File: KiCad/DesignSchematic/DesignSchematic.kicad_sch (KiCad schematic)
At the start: 17 parts, among them M1 Motor_DC, M2 Motor_DC, U1 EDU-CIAA, U2 AS5600, U3 AS5600, U4 MT3608, U5 VL53L0X, U6 DVR-8833, U7 MPU6050, U8 NodeMCU3.0(ESP-12E)

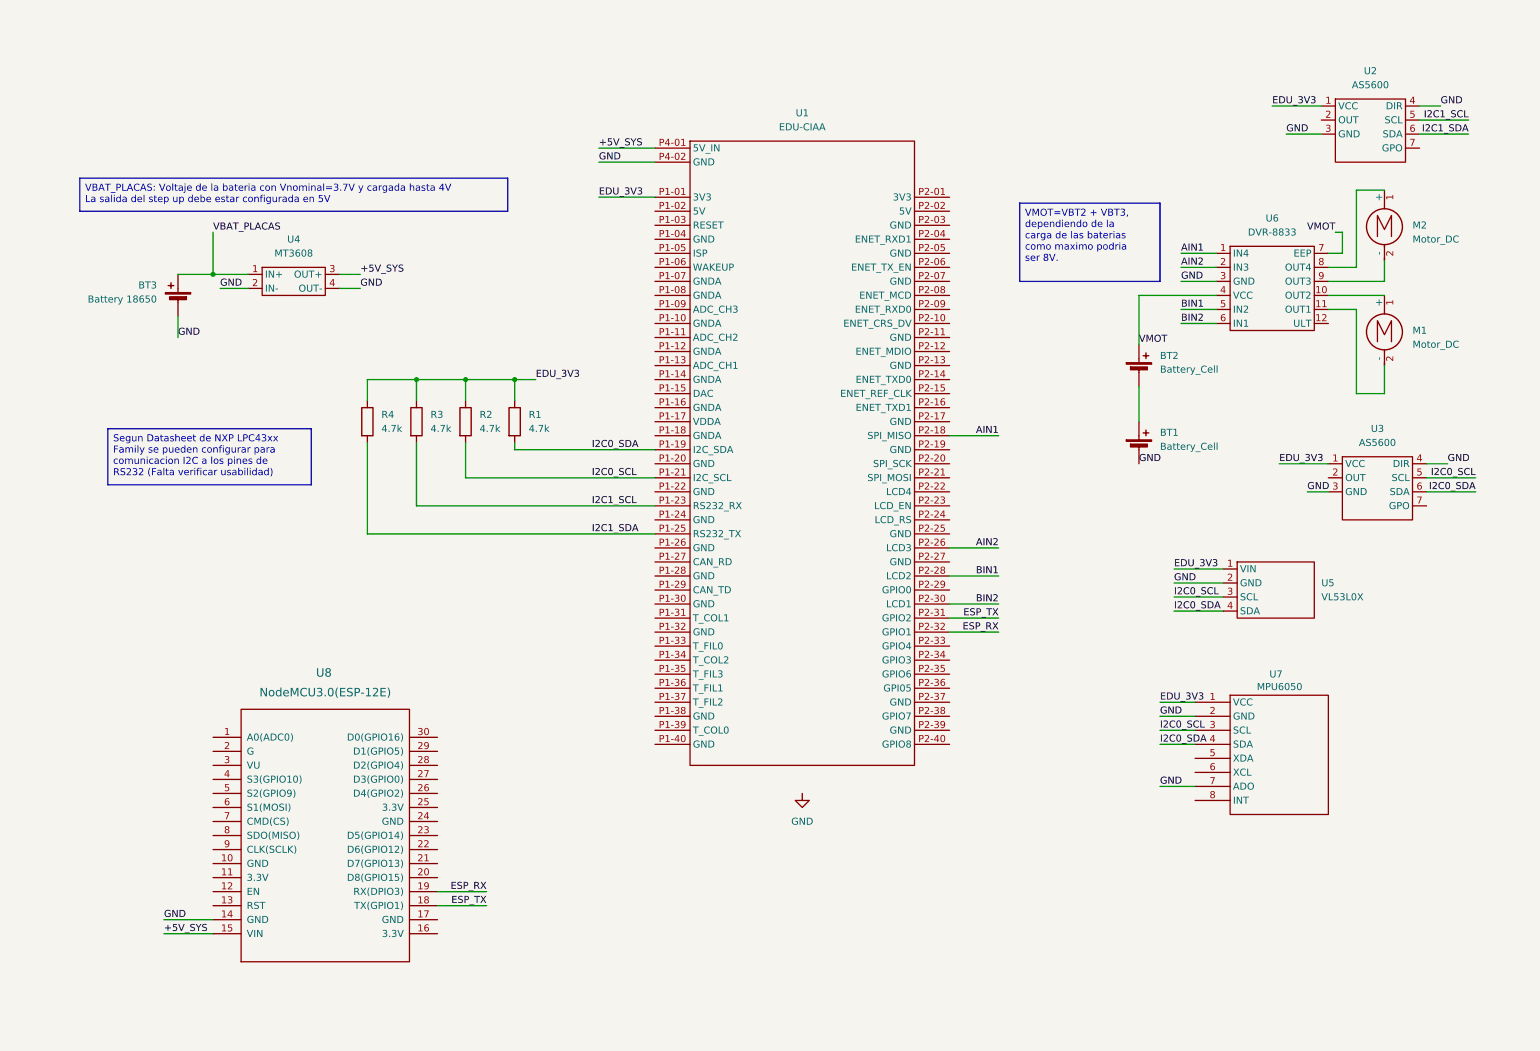
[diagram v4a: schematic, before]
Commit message: modificando esquematico
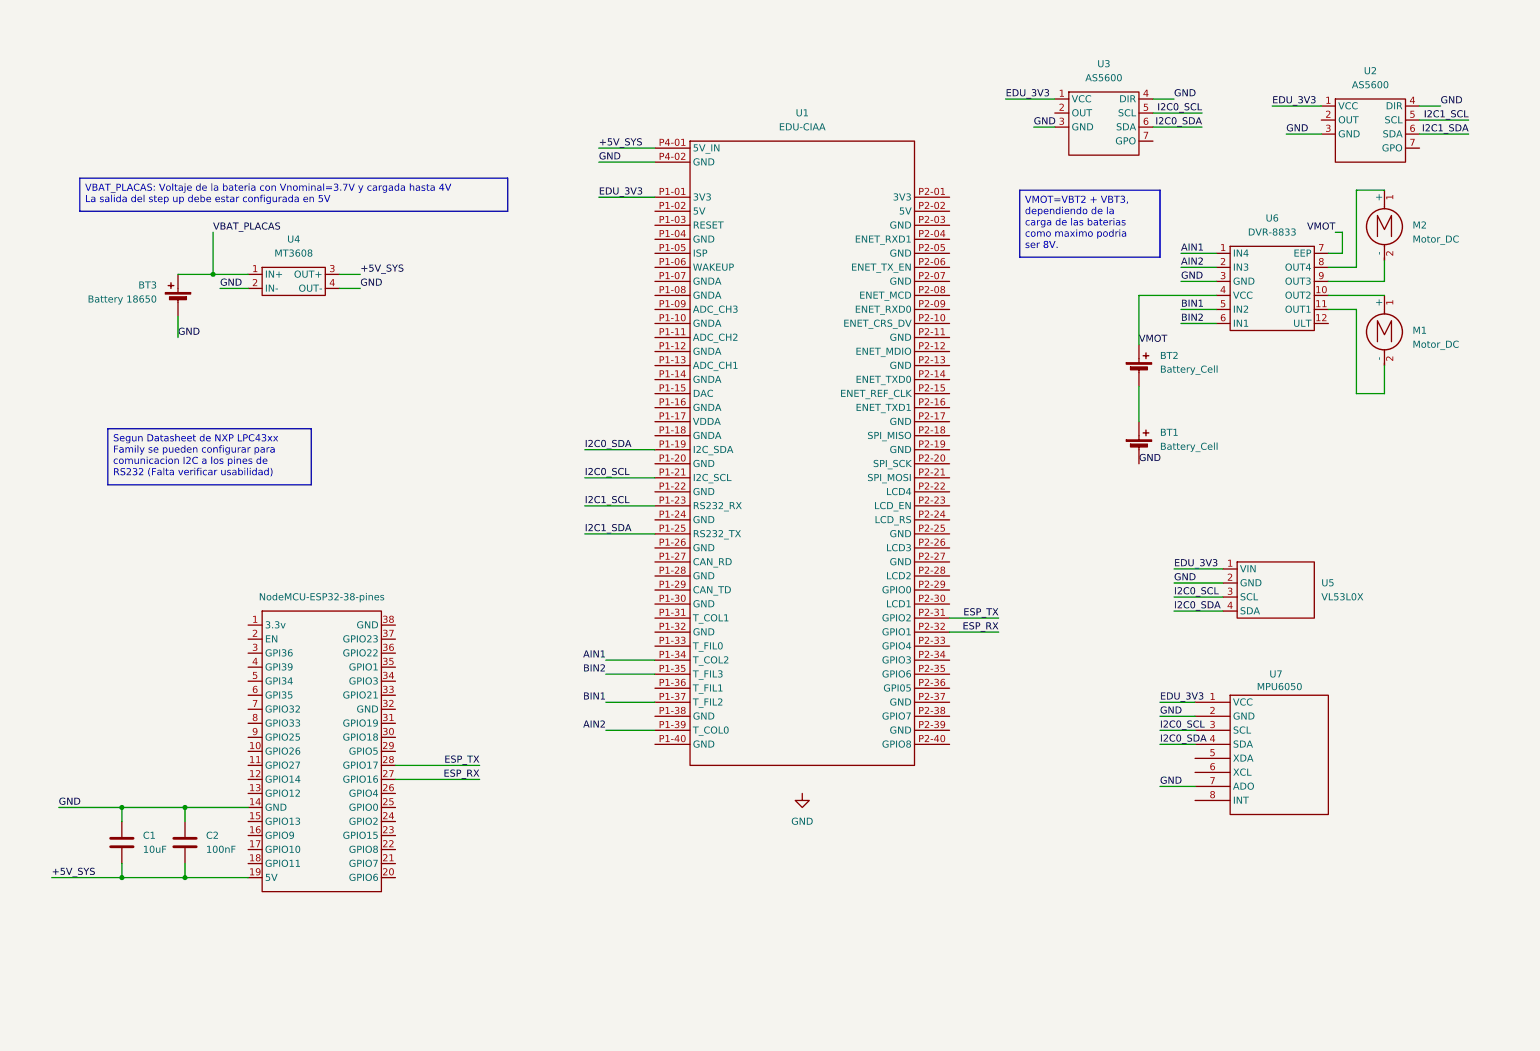
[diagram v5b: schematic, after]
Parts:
- removed R1, R2, R3, R4: 4.7k, Package_BGA:Microchip_TFBGA-196_11x11mm_Layout14x14_P0.75mm_SMD, symbol Device:R
- removed U8: NodeMCU3.0(ESP-12E), symbol Arturito:NodeMCU1.0(ESP-12E)
- added C1: 10uF, symbol Device:C
- added C2: 100nF, symbol Device:C
- added NodeMCU-ESP32-38-pines: (no value), symbol ESP32-38pin:Esp32
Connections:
- net +5V_SYS: now also C1.2, C2.2, NodeMCU-ESP32-38-pines.19 (5V)
- net AIN1: now also U1.P1-34 (T_COL2); no longer U1.P2-18 (SPI_MISO)
- net AIN2: now also U1.P1-39 (T_COL0); no longer U1.P2-26 (LCD3)
- net BIN1: now also U1.P1-37 (T_FIL2); no longer U1.P2-28 (LCD2)
- net BIN2: now also U1.P1-35 (T_FIL3); no longer U1.P2-30 (LCD1)
- net ESP_RX: now also NodeMCU-ESP32-38-pines.27 (GPIO16)
- net ESP_TX: now also NodeMCU-ESP32-38-pines.28 (GPIO17)
- net GND: now also C1.1, C2.1, NodeMCU-ESP32-38-pines.14 (GND)
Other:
- moved on the sheet: U3

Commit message: Organizacion Esquematico, chequear I2C y demas filtros o protecciones
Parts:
- added D1, D2: 1N5822, Diode_THT:D_DO-201AD_P15.24mm_Horizontal, symbol Diode:1N5822
- added SW1: SW_DPST, symbol Switch:SW_DPST
- BT1, BT2: value Battery_Cell -> Battery_18650
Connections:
- net +5V_SYS renamed +5V
- net EDU_3V3 renamed +3.3V
- net VBAT_PLACAS: no longer names the net of BT3.1 (+)
- net VBAT_PLACAS: now also D1.2 (A); no longer U4.1 (IN+)
- net VMOT renamed +7.4V
- net +7.4V: now also D2.2 (A), SW1.2
- new net: D2.1 (K), SW1.1
- new net: D1.1 (K), SW1.3
- new net +3.7V: SW1.4, U4.1 (IN+)
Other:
- note added: "Alimentación"
- note added: "Motores"
- note added: "Procesamiento Central"
- note added: "Sensado"
- note added: "Telemetria por Wi-Fi"
- moved on the sheet: BT1, BT2, BT3, C1, C2, M1, M2, NodeMCU-ESP32-38-pines, U1, U3, U4, U5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
